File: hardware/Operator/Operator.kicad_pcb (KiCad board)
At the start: 2 copper layers, 53.8 x 54.2 mm, 10 parts, among them J1 RJ45, J2 Screw_Terminal_01x02, J3 Conn_01x06_Male, U1 DS89C21

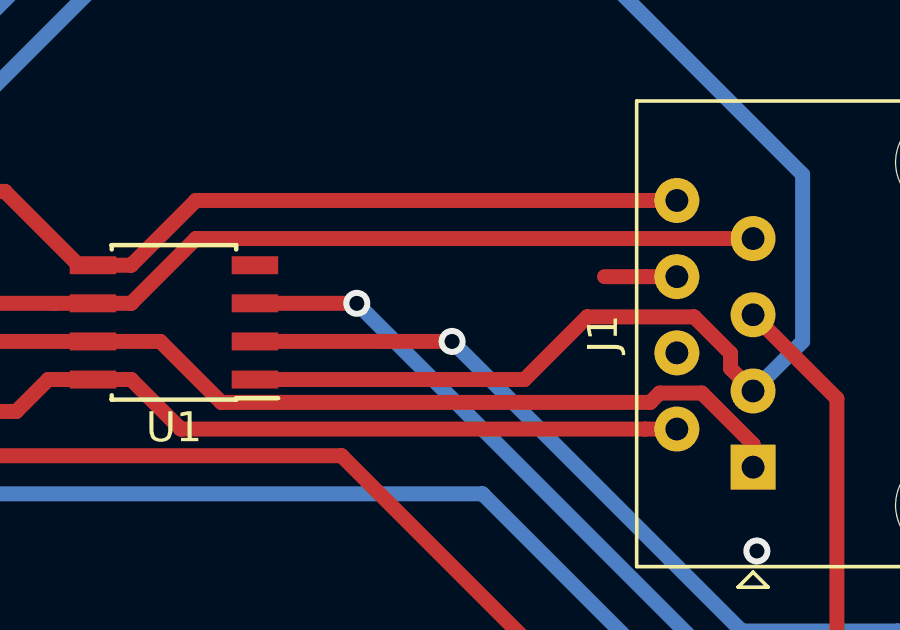
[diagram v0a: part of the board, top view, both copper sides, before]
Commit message: Added decoupling cap for rs485 chip
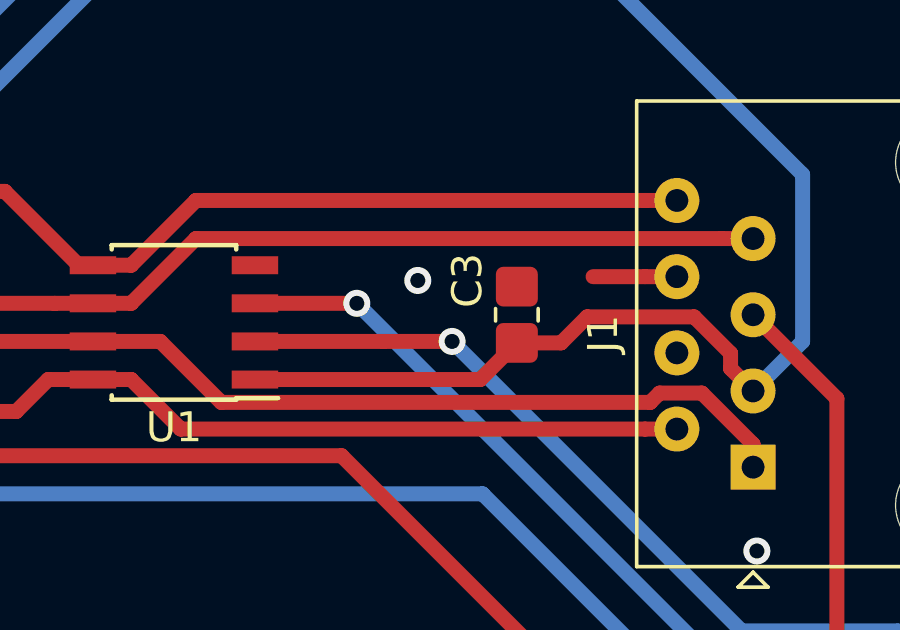
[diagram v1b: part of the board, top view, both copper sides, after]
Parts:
- added C3: 2.2nF, Capacitor_SMD:C_0805_2012Metric_Pad1.33x1.40mm_HandSolder, F.Cu at (165.6, 86.6)
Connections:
- A1 pad 1: (no net) -> Net-(A1-Pad1)
- A1 pad 10: (no net) -> Net-(A1-Pad10)
- A1 pad 11: (no net) -> Net-(A1-Pad11)
- A1 pad 12: (no net) -> Net-(A1-Pad12)
- A1 pad 19: (no net) -> Net-(A1-Pad19)
- A1 pad 2: (no net) -> Net-(A1-Pad2)
- A1 pad 21: (no net) -> Net-(A1-Pad21)
- A1 pad 22: (no net) -> Net-(A1-Pad22)
- A1 pad 23: (no net) -> Net-(A1-Pad23)
- A1 pad 24: (no net) -> Net-(A1-Pad24)
- A1 pad 25: (no net) -> Net-(A1-Pad25)
- A1 pad 26: (no net) -> Net-(A1-Pad26)
- A1 pad 27: (no net) -> Net-(A1-Pad27)
- A1 pad 28: (no net) -> Net-(A1-Pad28)
- A1 pad 3: (no net) -> Net-(A1-Pad3)
- A1 pad 30: (no net) -> Net-(A1-Pad30)
- A1 pad 31: (no net) -> Net-(A1-Pad31)
- A1 pad 32: (no net) -> Net-(A1-Pad32)
- A1 pad 4: (no net) -> Net-(A1-Pad4)
- A1 pad 8: (no net) -> Net-(A1-Pad8)
- J1 pad 4: (no net) -> Net-(J1-Pad4)
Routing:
- net /GND: track 2.41 -> 2.79 mm, vias 2 -> 3
